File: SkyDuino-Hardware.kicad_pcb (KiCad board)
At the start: 2 copper layers, 123 x 56 mm, 77 parts, among them J1 PWR, J11 DBG, J12 USB-A RMT, J13 DISP, J14 USB_C Artisan, J2 BT, J4 Drum, J5 Exhaust, J6 Cooling, J7 Cooling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

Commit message: Add 3d Models
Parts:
- moved R15 147.5 mm to (223.5, 110.5)
- moved R16 147.0 mm to (223.5, 112.5)
- moved R19 141.2 mm to (223.5, 108.5)
- moved R18 125.3 mm to (205.0, 107.0)
- moved R17 125.3 mm to (205.0, 104.0)
- moved R13 123.7 mm to (196.0, 103.5), turned to 180 degrees
- moved R14 123.2 mm to (196.0, 105.5), turned to 180 degrees
- moved C19 112.5 mm to (184.5, 125.5)
- moved C20 112.4 mm to (189.5, 123.0)
- moved C12 111.6 mm to (179.5, 123.0)
- moved C14 109.3 mm to (191.5, 106.0)
- moved C17 108.3 mm to (184.5, 123.0)
- moved C15 103.9 mm to (187.0, 106.0)
- moved C13 95.4 mm to (181.0, 106.0)
- moved C16 94.1 mm to (176.5, 107.0)
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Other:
- rule pad_to_mask_clearance: 0 -> 0.038

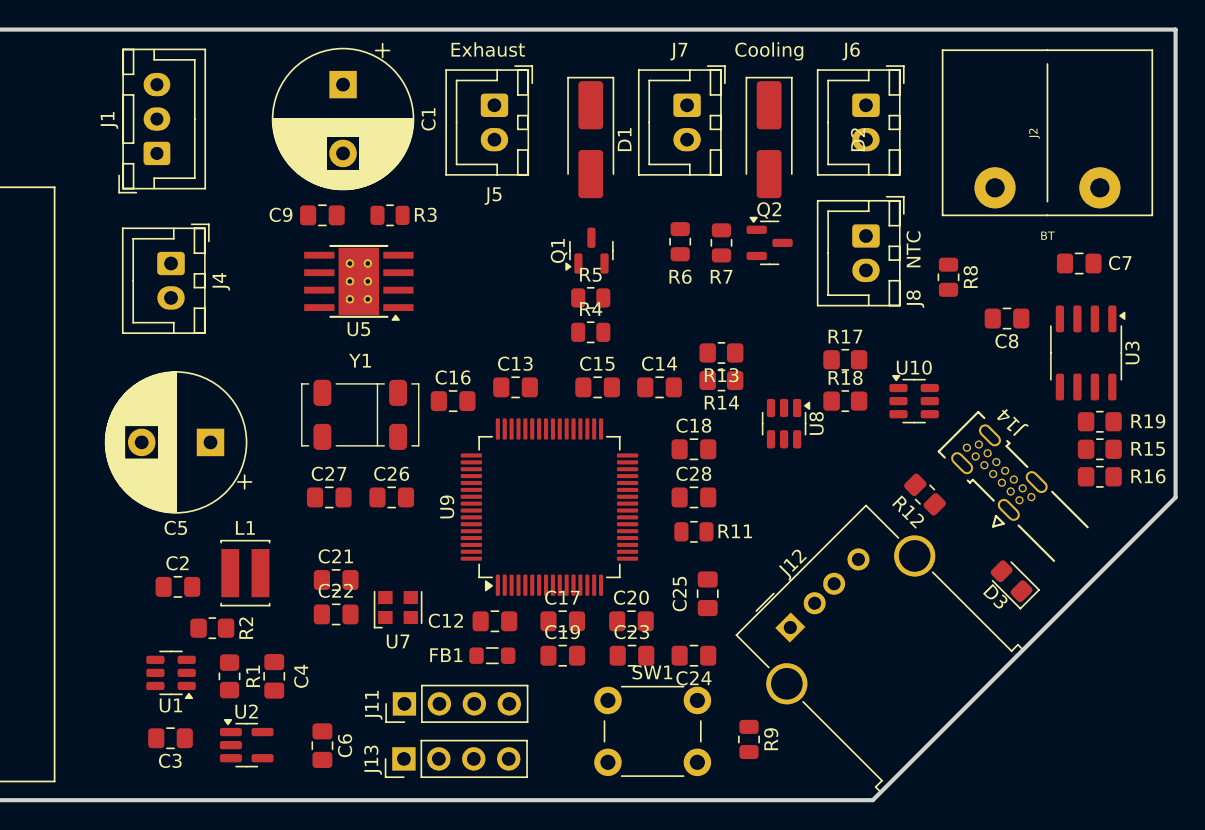
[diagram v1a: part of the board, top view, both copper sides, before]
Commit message: Rearrange components. Fix 25MHz oscillator connection
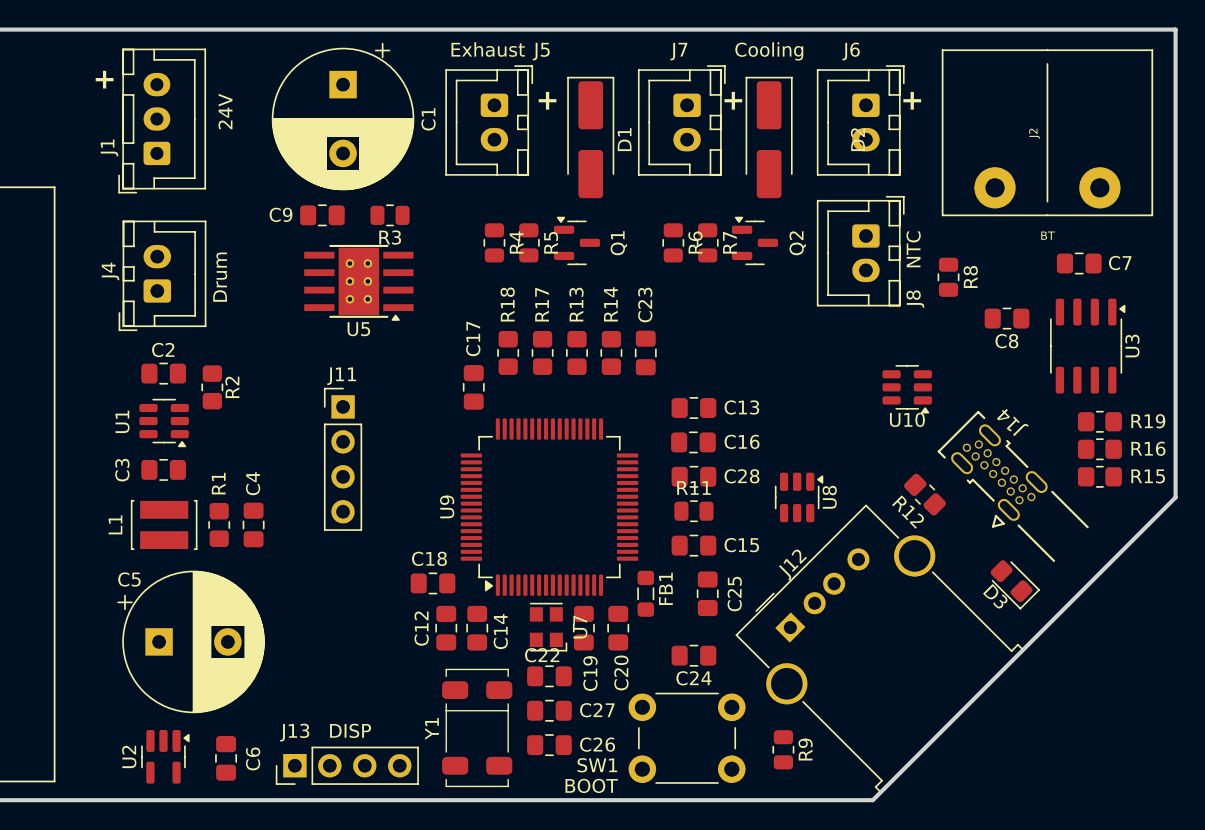
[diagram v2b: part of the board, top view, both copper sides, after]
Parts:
- removed C21: 11pF, Capacitor_SMD:C_0805_2012Metric_Pad1.18x1.45mm_HandSolder
- J1: value PWR -> 24V
- moved R18 24.7 mm to (180.5, 103.5), turned to -90 degrees
- moved Y1 24.3 mm to (178.2, 130.8), turned to -90 degrees
- moved C27 22.3 mm to (183.5, 129.5), turned to 180 degrees
- moved J11 22.0 mm to (168.5, 107.4), turned to 0 degrees
- moved C23 22.0 mm to (190.5, 103.5), turned to 90 degrees
- moved R17 22.0 mm to (183.0, 103.5), turned to -90 degrees
- moved C14 22.0 mm to (178.2, 123.5), turned to -90 degrees
- moved C26 21.3 mm to (183.5, 132.0), turned to 180 degrees
- moved C18 21.3 mm to (175.0, 120.2), turned to 180 degrees
- moved C3 19.5 mm to (155.5, 112.0)
- moved U1 18.3 mm to (155.5, 108.5)
- moved C17 18.2 mm to (178.0, 106.0), turned to 90 degrees
- moved C16 17.7 mm to (194.0, 110.0)
- moved R2 17.5 mm to (159.0, 106.0), turned to 90 degrees
- moved C22 16.1 mm to (183.5, 127.0)
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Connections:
- net Net-(U9-PC14) renamed /CPU/XTAL_32K768_1
- net Net-(U9-PC15) renamed /CPU/XTAL_32K768_2
- net Net-(U9-VDDA) renamed /CPU/VDDA
- C22 pad 1: Net-(U7-INH) -> /CPU/XTAL_25M_1
- U5 pad 6: Net-(J4-Pin_1) -> Net-(J4-Pin_2)
- U5 pad 8: Net-(J4-Pin_2) -> Net-(J4-Pin_1)
- U7 pad 1: Net-(U7-INH) -> +3V3
- U7 pad 3: Net-(U7-CLK) -> /CPU/XTAL_25M_1
- U9 pad 5: Net-(U7-CLK) -> /CPU/XTAL_25M_1
- U9 pad 6: Net-(U7-INH) -> unconnected-(U9-PH1-Pad6)
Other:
- copper layers 2 -> 4
- board text added: "+"

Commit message: WIP PCB tracing
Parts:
- moved R15 12.9 mm to (210.6, 113.6), turned to 135 degrees
- moved J14 7.66 mm to (216.1, 112.1)
- moved R12 4.25 mm to (213.8, 116.8)
- moved R19 4.10 mm to (223.5, 112.6)
- moved Q2 1.88 mm to (196.6, 95.5)
- moved R6 1.88 mm to (190.6, 95.5)
- moved R7 1.88 mm to (193.1, 95.5)
- moved Q1 1.44 mm to (184.1, 95.5)
- moved R4 1.44 mm to (178.1, 95.5)
- moved R5 1.44 mm to (180.6, 95.5)
- moved C8 0.50 mm to (216.8, 100.5)
- turned R8 to 90 degrees
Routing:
- net Net-(R18-Pad1): track 0.00 -> 32.4 mm
- net Net-(R17-Pad1): track 0.00 -> 31.3 mm
- net Net-(R13-Pad1): track 0.00 -> 30.6 mm
- net Net-(R14-Pad1): track 0.00 -> 25.6 mm
- net Net-(J14-SHIELD): track 0.00 -> 20.9 mm, vias 0 -> 1
- net /CPU/D-: track 0.00 -> 20.9 mm, vias 0 -> 2
- net EXHT: track 0.00 -> 14.4 mm
- net /CPU/D+: track 0.00 -> 13.7 mm, vias 0 -> 1
- net COOL: track 0.00 -> 13.5 mm
- net Net-(J2-Pin_1): track 0.00 -> 12.3 mm
- net Net-(J2-Pin_2): track 0.00 -> 9.29 mm
- net +3V3: track 0.00 -> 8.76 mm
- net FROM_RMT: track 0.00 -> 7.64 mm
- net Net-(J12-D-): track 0.00 -> 7.47 mm
- net Net-(J14-CC2): track 0.00 -> 6.93 mm
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
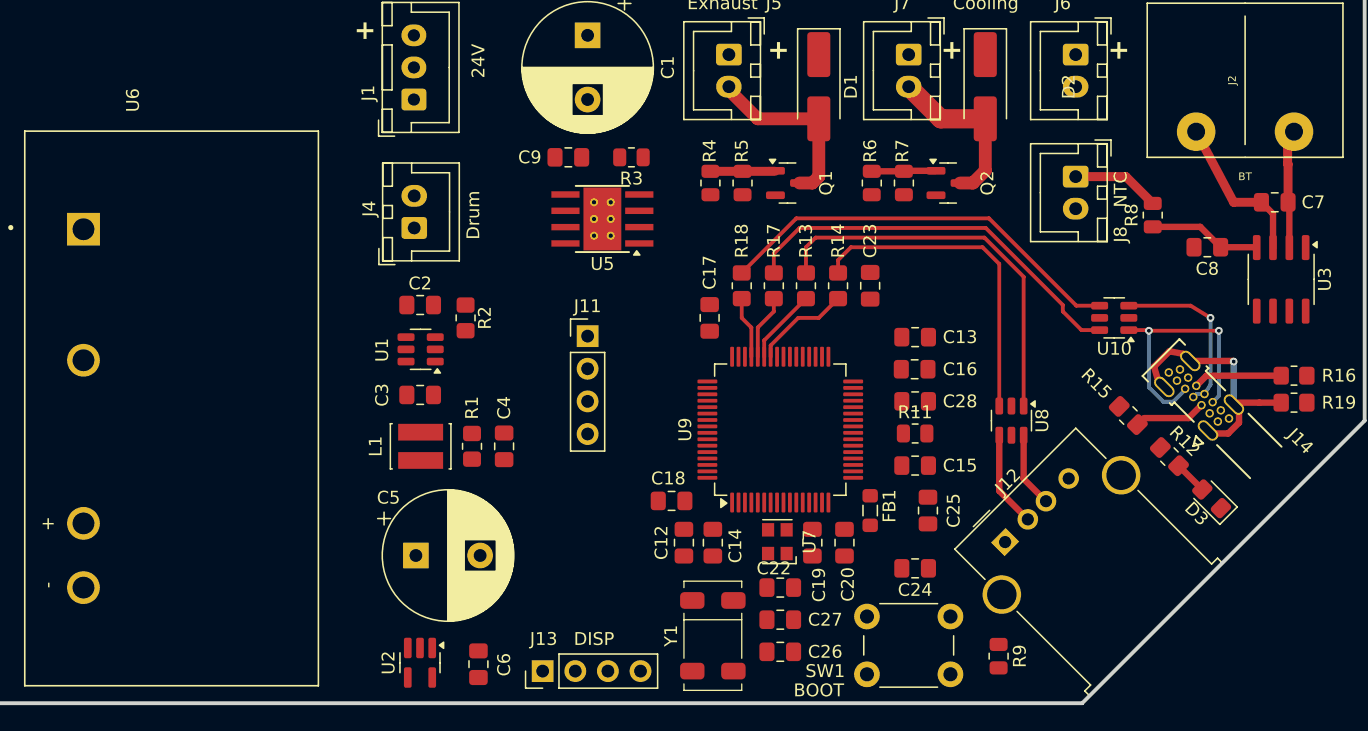
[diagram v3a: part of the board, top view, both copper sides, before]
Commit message: PCB Signalling routing
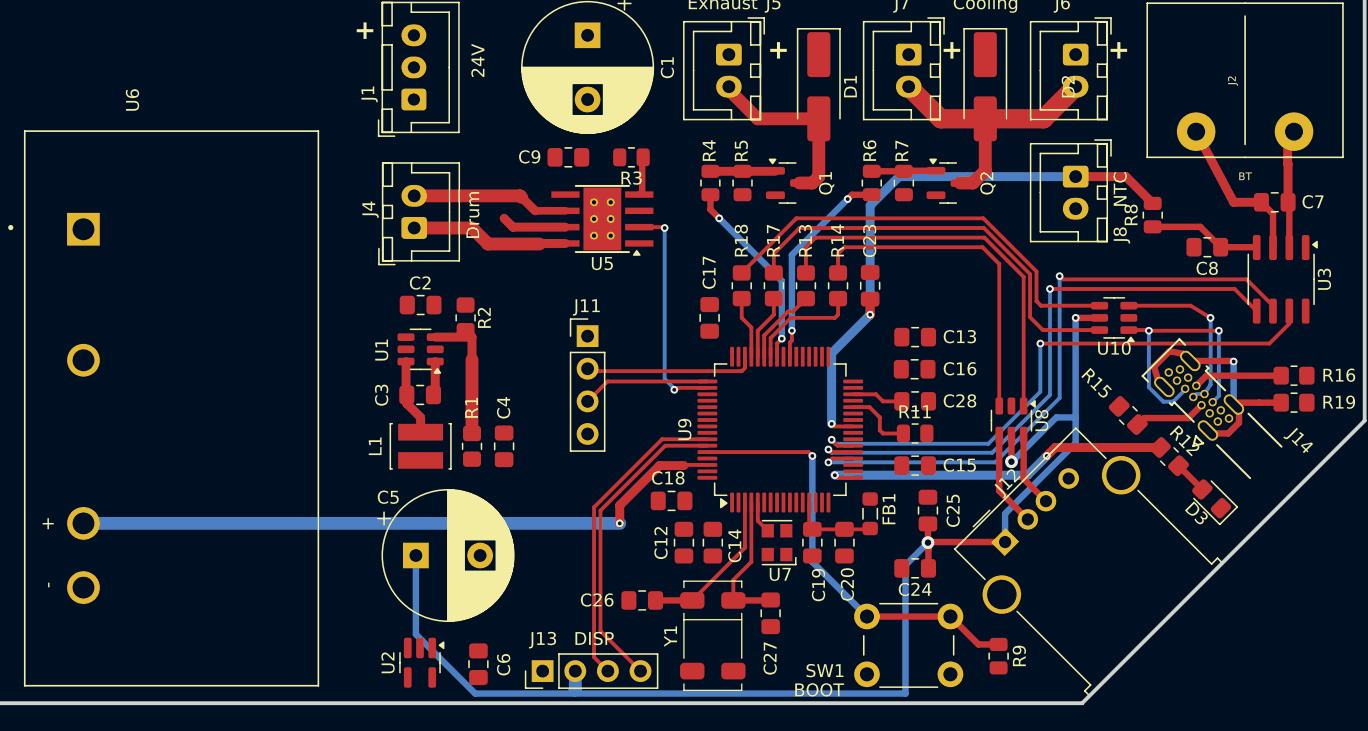
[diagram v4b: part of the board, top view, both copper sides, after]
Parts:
- removed C22: 11pF, Capacitor_SMD:C_0805_2012Metric_Pad1.18x1.45mm_HandSolder
- moved C26 11.5 mm to (172.8, 128.0), turned to 0 degrees
- moved C27 0.90 mm to (182.8, 129.0), turned to 90 degrees
- moved FB1 0.25 mm to (190.5, 121.2)
- moved U7 0.08 mm to (183.2, 123.5)
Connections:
- U9 pad 10: COOL_CTL -> unconnected-(U9-PC2-Pad10)
- U9 pad 11: SSR -> unconnected-(U9-PC3-Pad11)
- U9 pad 14: LED0 -> unconnected-(U9-PA0-Pad14)
- U9 pad 15: NTC -> unconnected-(U9-PA1-Pad15)
- U9 pad 17: ETCS -> LED0
- U9 pad 25: unconnected-(U9-PC5-Pad25) -> NTC
- U9 pad 39: unconnected-(U9-PC8-Pad39) -> COOL_CTL
- U9 pad 41: unconnected-(U9-PA8-Pad41) -> EXHT_CTL
- U9 pad 50: unconnected-(U9-PA15-Pad50) -> DRUM_CTL
- U9 pad 62: unconnected-(U9-PB9-Pad62) -> SSR
- U9 pad 8: DRUM_CTL -> unconnected-(U9-PC0-Pad8)
- U9 pad 9: EXHT_CTL -> unconnected-(U9-PC1-Pad9)
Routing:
- net +5V: track 0.00 -> 99.7 mm, vias 0 -> 3
- net SSR: track 0.00 -> 51.3 mm, vias 0 -> 1
- net BTCS: track 0.00 -> 49.6 mm, vias 0 -> 2
- net SCK: track 0.00 -> 46.3 mm, vias 0 -> 2
- net SO: track 0.00 -> 44.7 mm, vias 0 -> 2
- net NTC: track 6.86 -> 45.0 mm, vias 0 -> 2
- net BOOT0: track 0.00 -> 33.7 mm, vias 0 -> 1
- net LED0: track 0.00 -> 27.7 mm, vias 0 -> 2
- net SCL: track 0.00 -> 24.2 mm
- net SDA: track 0.00 -> 24.2 mm
- net DRUM_CTL: track 0.00 -> 17.5 mm, vias 0 -> 2
- net COOL_CTL: track 0.00 -> 16.2 mm, vias 0 -> 2
- net EXHT_CTL: track 0.00 -> 15.1 mm, vias 0 -> 2
- net SWDIO: track 0.00 -> 13.3 mm
- net Net-(J4-Pin_1): track 0.00 -> 12.3 mm
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
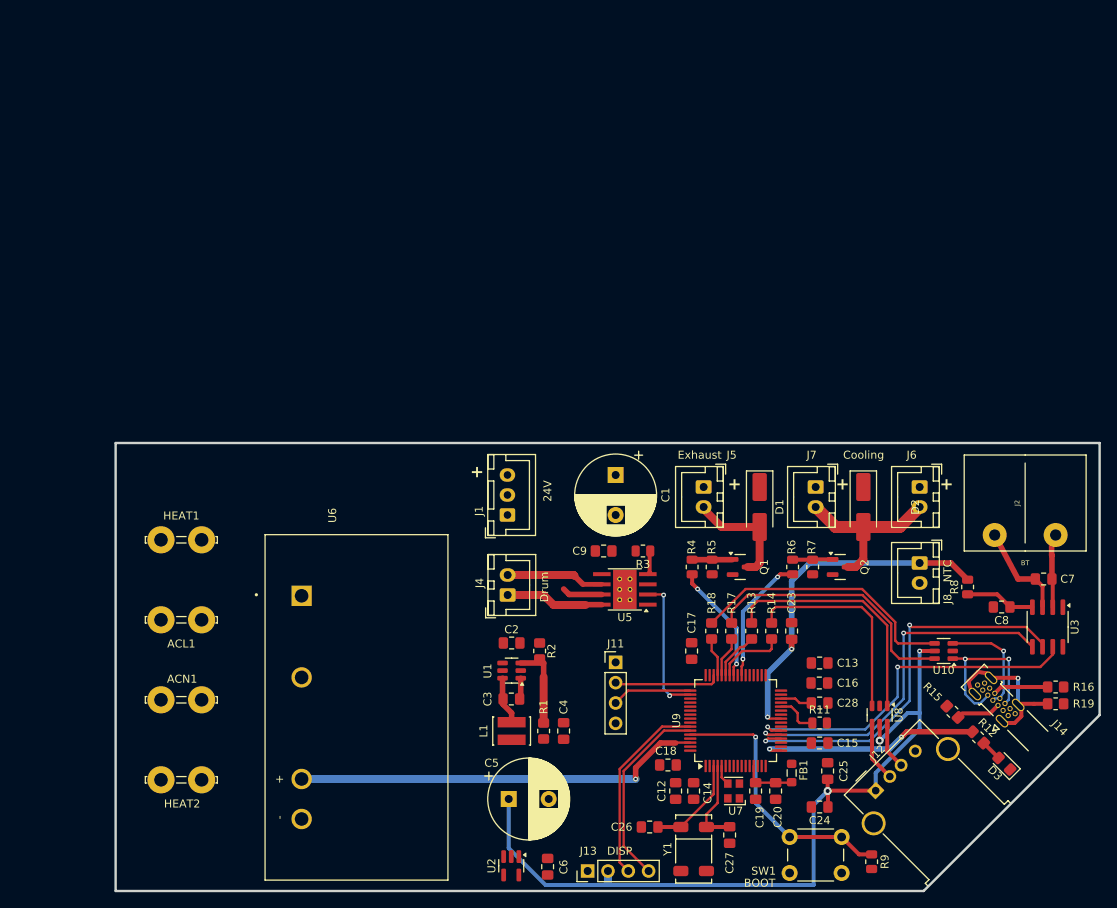
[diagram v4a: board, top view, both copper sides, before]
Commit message: Copper fill for power
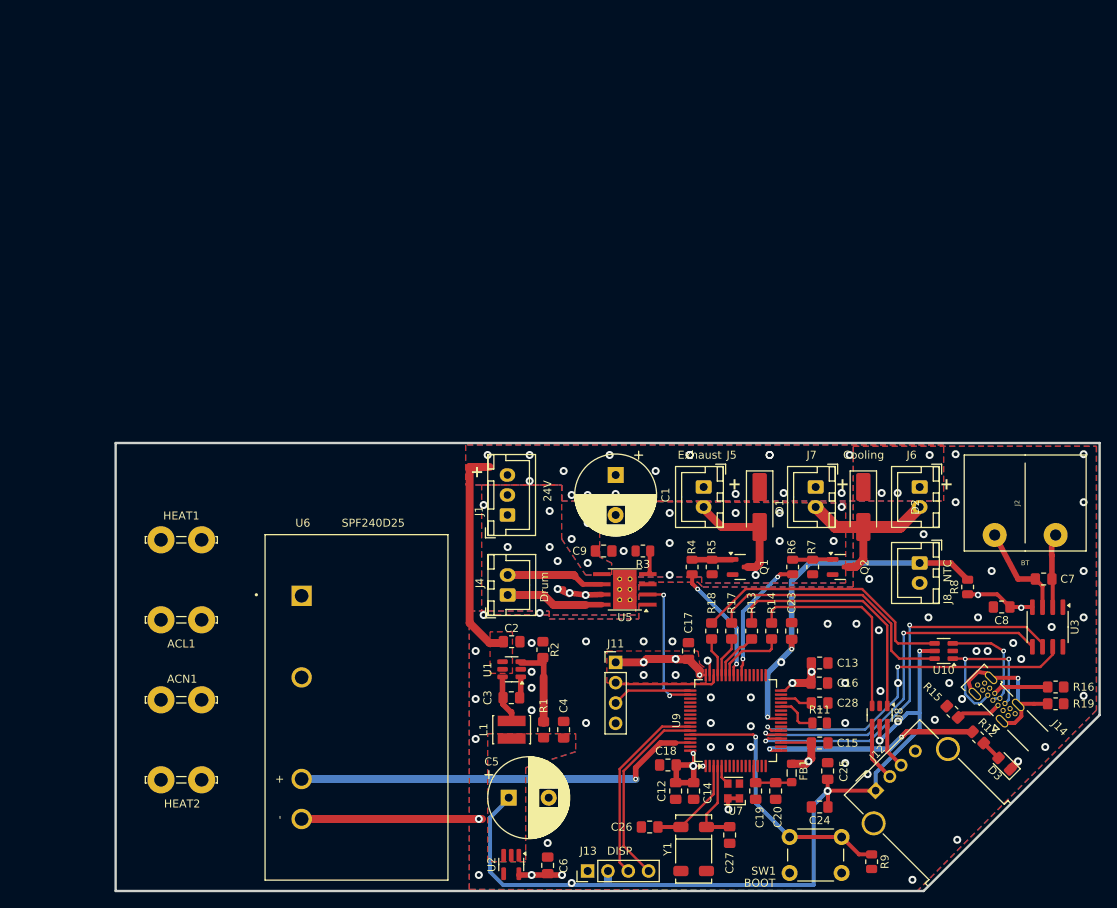
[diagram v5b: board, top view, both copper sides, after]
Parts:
- moved R2 0.43 mm to (159.4, 105.8)
- moved C17 0.40 mm to (177.6, 106.0)
- moved U1 0.16 mm to (155.5, 108.3)
- moved C2 0.16 mm to (155.5, 104.8)
- moved C3 0.16 mm to (155.5, 111.8)
- moved C4 0.16 mm to (162.0, 115.8)
- moved C5 0.16 mm to (155.1, 124.3)
- moved C6 0.16 mm to (160.0, 132.8)
- moved L1 0.16 mm to (155.5, 115.8)
- moved R1 0.16 mm to (159.5, 115.8)
- moved U2 0.16 mm to (155.4, 132.7)
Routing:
- net +3V3: track 8.76 -> 59.1 mm, vias 0 -> 16
- net GND: track 5.06 -> 32.5 mm, vias 0 -> 78
- net +24V: track 0.00 -> 27.2 mm, vias 0 -> 23
- net +5V: track 99.7 -> 104.8 mm
- net Net-(ACN1-Pin_1): track 0.00 -> 1.00 mm
- added copper zone on B.Cu, net +24V
- added copper zone on F.Cu, net +24V
- added copper zone on In1.Cu, net +24V
- added copper zone on In2.Cu, net +24V
- added copper zone on F.Cu, net +3V3
- added copper zone on In1.Cu, net +3V3
- added copper zone on B.Cu, net +5V
- added copper zone on F.Cu, net +5V
- added copper zone on B.Cu, net GND
- added copper zone on F.Cu, net GND
- added copper zone on In1.Cu, net GND
- added copper zone on In2.Cu, net GND
